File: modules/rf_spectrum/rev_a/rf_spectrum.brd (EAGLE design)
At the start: 68.1 x 66 mm, 41 parts, among them J1 MODULE_GENERIC_DEBUGSMT, J7 TC2030-JLINK-L, U1 STM32L432KC, U2 MWSUB3G, U3 SKY13317, U7 TLV62130, X2 ABS05-32.768KHZ-9-T

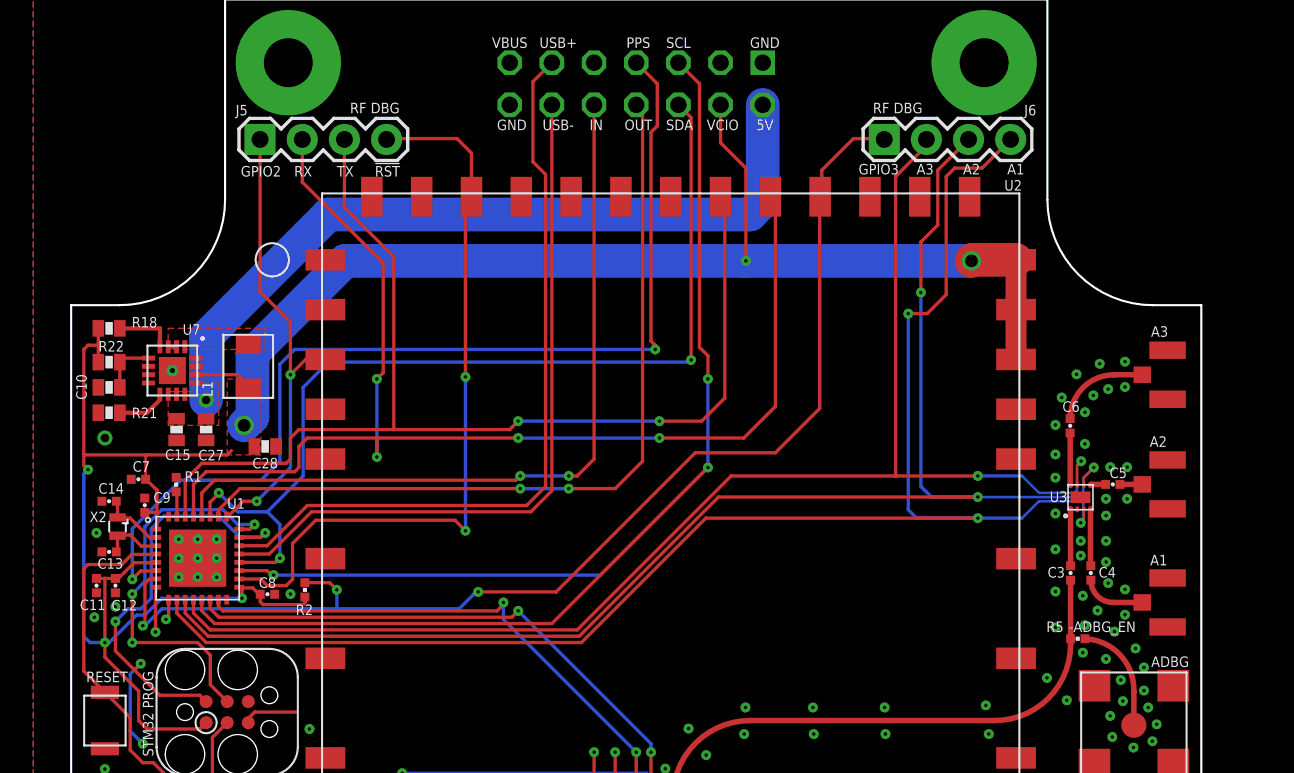
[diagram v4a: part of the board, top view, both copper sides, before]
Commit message: renumbered parts
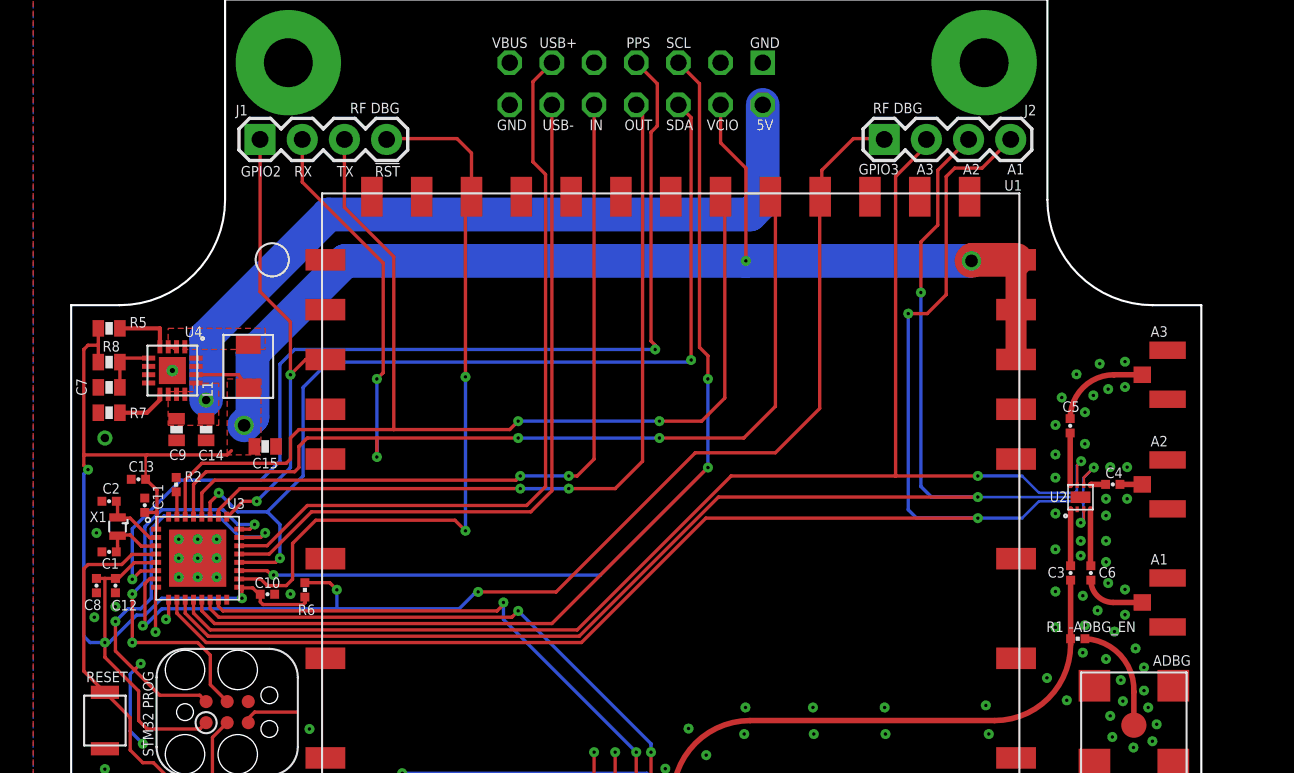
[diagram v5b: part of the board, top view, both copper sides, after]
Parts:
- removed C27: 10uF, passives:0603_CAP
- removed C28: 22uF, passives:0603_CAP
- removed J5: (no value), SparkFun-Connectors:1X04
- removed R18: 100k, passives:0603-RES
- added C1, C2: 4.3pF, passives:0402_CAP
- added J3: MODULE_GENERIC_DEBUGSMT, signpost:MODULE_GENERIC_DEBUG_SMT
- added R6: 100k, passives:0402_RES
- C10: value 3.3nF -> 100nF; device passives:0603_CAP -> passives:0402_CAP
- C11: value 10nF -> 100nF
- C13: value 4.3pF -> 4.7uF
- C14: value 4.3pF -> 10uF; device passives:0402_CAP -> passives:0603_CAP
- C15: value 0.1uF -> 22uF
- C4: value 220pF -> 47pF
- C6: value 47pF -> 220pF
- C7: value 4.7uF -> 3.3nF; device passives:0402_CAP -> passives:0603_CAP
- C8: value 100nF -> 10nF
- C9: value 100nF -> 0.1uF; device passives:0402_CAP -> passives:0603_CAP
- J1: value MODULE_GENERIC_DEBUGSMT -> (none); device signpost:MODULE_GENERIC_DEBUG_SMT -> SparkFun-Connectors:1X04
- R1: value 10k -> 0
- R2: value 100k -> 10k
- R5: value 0 -> 100k; device passives:0402_RES -> passives:0603-RES
- U1: value STM32L432KC -> MWSUB3G; device chips:UQFN-32 -> signpost:MWSUB3G
- U2: value MWSUB3G -> SKY13317; device signpost:MWSUB3G -> chips:XDFN-8
- U3: value SKY13317 -> STM32L432KC; device chips:XDFN-8 -> chips:UQFN-32
- moved R5 61.3 mm to (4.83, 48.8), turned to 180 degrees
- moved R1 55.1 mm to (63.2, 30.1), turned to 0 degrees
- moved U3 54.0 mm to (10.2, 34.9), turned to 0 degrees
- moved U2 50.2 mm to (64.1, 37.8), turned to 90 degrees
- moved J1 33.4 mm to (13.9, 60.1)
- moved U1 23.2 mm to (17.7, 56.9), turned to 270 degrees
- moved C10 14.5 mm to (14.4, 32.8)
- moved C8 10.3 mm to (4.06, 33.3), turned to 270 degrees
- moved R2 10.0 mm to (8.87, 39.4)
- moved C6 8.95 mm to (64.0, 34.0), turned to 270 degrees
- moved C14 7.26 mm to (10.7, 42.7), turned to 270 degrees
- moved C11 5.65 mm to (6.97, 38.1), turned to 90 degrees
- moved C4 5.50 mm to (65.3, 39.4), turned to 180 degrees
- moved C15 5.43 mm to (14.2, 41.7), turned to 180 degrees
- moved C9 4.95 mm to (8.89, 42.7), turned to 270 degrees
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- renumbered J6 to J2, J7 to J4, R21 to R7, R22 to R8, U7 to U4, X2 to X1
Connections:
- net !RF_RESET: now also J1.4, U1.P$44, U3.P$18; no longer J5.4, U1.P$18, U2.P$44
- net !RST: now also J3.20, U3.P$4; no longer J1.20, U1.P$4
- net 3V3: now also C10.1, C13.1, C15.2, J3.4, R5.2, R6.2, U1.P$31, U1.P$32, U1.P$33, U3.P$1, U3.P$17, U3.P$5; no longer C28.2, C7.1, C9.1, J1.4, R18.2, R2.2, U1.P$1, U1.P$17, U1.P$5, U2.P$31, U2.P$32, U2.P$33
- net 5V: now also C14.1, C9.1, J3.2; no longer C15.1, C27.1, J1.2
- net DBG_GPIO1: now also J3.16, U3.P$14; no longer J1.16, U1.P$14
- net DBG_GPIO2: now also J3.19, U3.P$15; no longer J1.19, U1.P$15
- net DBG_RX: now also J3.18, U3.P$9; no longer J1.18, U1.P$9
- net DBG_TX: now also J3.17, U3.P$8; no longer J1.17, U1.P$8
- net GND: now also C1.2, C10.2, C15.1, C2.2, C7.1, J3.1, J3.14, J3.15, R2.1, U1.P$10, U1.P$11, U1.P$12, U1.P$13, U1.P$14, U1.P$15, U1.P$18, U1.P$20, U1.P$21, U1.P$22, U1.P$24, U1.P$26, U1.P$27, U1.P$28, U1.P$29, U1.P$34, U1.P$43, U1.P$45, U1.P$46, U1.P$5, U1.P$6, U1.P$7, U1.P$8, U1.P$9, U2.P$1, U3.P$16, U3.P$32, U3.P$33; no longer C10.1, C15.2, C27.2, C28.1, C7.2, J1.1, J1.14, J1.15, R1.1, U1.P$32, U1.P$33, U2.P$10, U2.P$11, U2.P$12, U2.P$13, U2.P$14, U2.P$15, U2.P$16, U2.P$18, U2.P$20, U2.P$21, U2.P$22, U2.P$24, U2.P$26, U2.P$27, U2.P$28, U2.P$29, U2.P$34, U2.P$43, U2.P$45, U2.P$46, U2.P$5, U2.P$6, U2.P$7, U2.P$8, U2.P$9, U3.P$1
- net MOD_IN: now also J3.10, U3.P$28; no longer J1.10, U1.P$28
- net MOD_OUT: now also J3.8, U3.P$26; no longer J1.8, U1.P$26
- net N$1: now also R1.1, U1.P$17; no longer R5.1, U2.P$17
- net N$10: now also C1.1, U3.P$3; no longer C13.1, U1.P$3
- net N$11: now also R2.2, U3.P$31; no longer R1.2, U1.P$31
- net N$14: now also R1.2; no longer R5.2
- net N$2: now also U2.1; no longer U3.1
- net N$3: now also C6.1, U2.4; no longer C4.1, U3.4
- net N$34: now also C7.2; no longer C10.2
- net N$36: now also R5.1; no longer R18.1
- net N$4: now also C6.2; no longer C4.2
- net N$5: now also C4.2, U2.5; no longer C5.2, U3.5
- net N$6: now also C4.1; no longer C5.1
- net N$7: now also C5.1, U2.8; no longer C6.1, U3.8
- net N$8: now also C5.2; no longer C6.2
- net N$9: now also C2.1, U3.P$2; no longer C14.1, U1.P$2
- net PPS: now also J3.7, U3.P$6; no longer J1.7, U1.P$6
- net RF_ANT1: now also U2.3, U3.P$10; no longer U1.P$10, U3.3
- net RF_ANT2: now also U2.6, U3.P$11; no longer U1.P$11, U3.6
- net RF_ANT3: now also U2.7, U3.P$12; no longer U1.P$12, U3.7
- net RF_GPIO2: now also J1.1, U1.P$3, U3.P$25; no longer J5.1, U1.P$25, U2.P$3
- net RF_GPIO3: now also R6.1, U1.P$37, U3.P$7; no longer R2.1, U1.P$7, U2.P$37
- net RF_RX: now also J1.2, U1.P$38, U3.P$29; no longer J5.2, U1.P$29, U2.P$38
- net RF_TX: now also J1.3, U1.P$39, U3.P$30; no longer J5.3, U1.P$30, U2.P$39
- net SCL: now also J3.5, U3.P$13, U3.P$19; no longer J1.5, U1.P$13, U1.P$19
- net SDA: now also J3.6, U3.P$20, U3.P$27; no longer J1.6, U1.P$20, U1.P$27
- net SWDCLK: now also J3.21, U3.P$24; no longer J1.21, U1.P$24
- net SWDIO: now also J3.22, U3.P$23; no longer J1.22, U1.P$23
- net USB+: now also J3.11, U3.P$22; no longer J1.11, U1.P$22
- net USB-: now also J3.12, U3.P$21; no longer J1.12, U1.P$21

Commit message: added part numbers
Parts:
- R2, R3: value 10k -> 1k
- X1: value ABS05-32.768KHZ-9-T -> ABS05-32.768KHZ-T
- moved R2 31.0 mm to (15.7, 9.14), turned to 90 degrees
- moved R4 30.6 mm to (8.87, 39.4), turned to 270 degrees
- moved R3 2.29 mm to (13.5, 9.14)
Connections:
- removed net N$13: D2.A, R4.1
- new net R3: D2.A, R3.1
- new net R4: R4.1
- net DBG_GPIO1: now also R2.2; no longer R3.2
- net DBG_GPIO2: now also R3.2; no longer R4.2
- net GND: no longer R2.1
- net N$11: now also R4.2; no longer R2.2
- net N$12: now also R2.1; no longer R3.1
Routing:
- net R3: track 0.00 -> 1.36 mm
- net N$13: track 1.36 -> 0.00 mm
